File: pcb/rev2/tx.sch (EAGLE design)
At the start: 54 parts, among them U3 MCP73831T-2ACI/OT, Y1 CRYSTAL-26MHZSMD-3.2X2.5

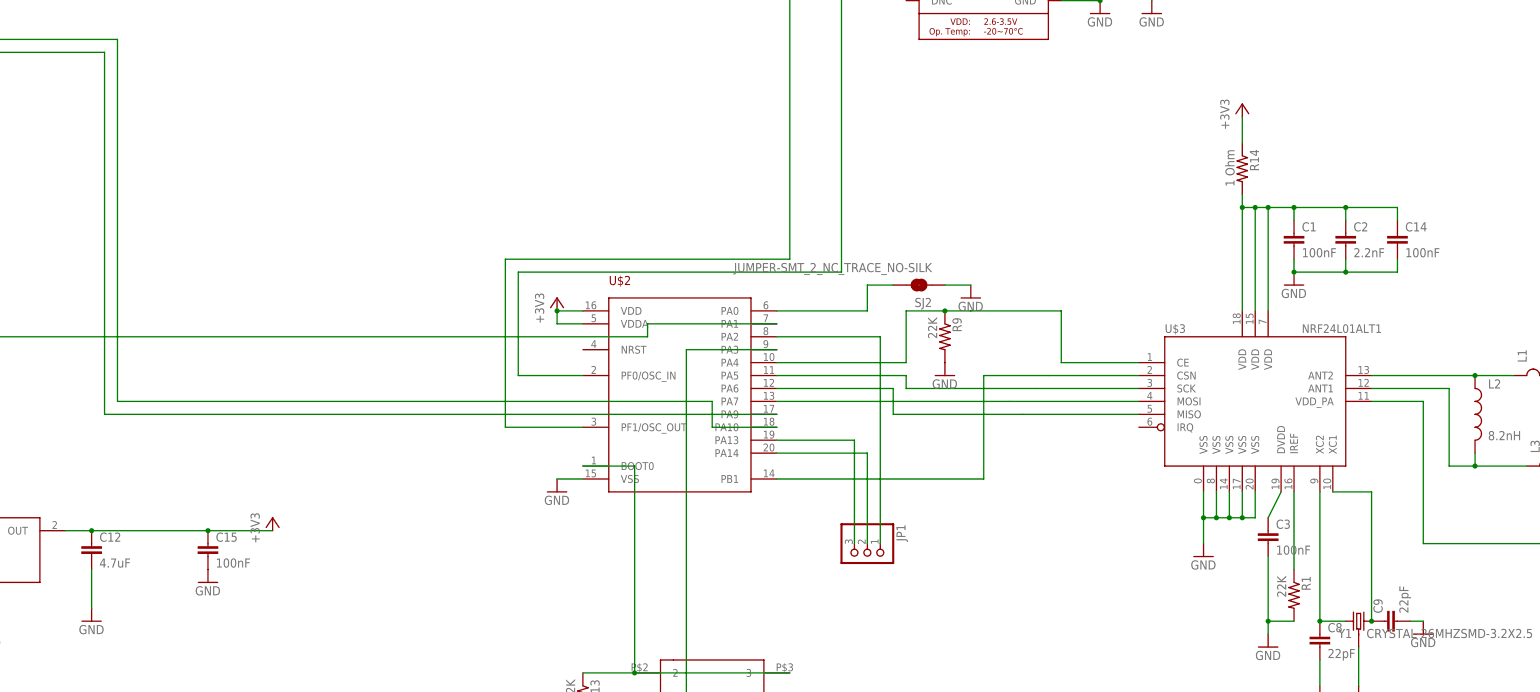
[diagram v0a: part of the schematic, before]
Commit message: added more power filtering, added RX interrupt
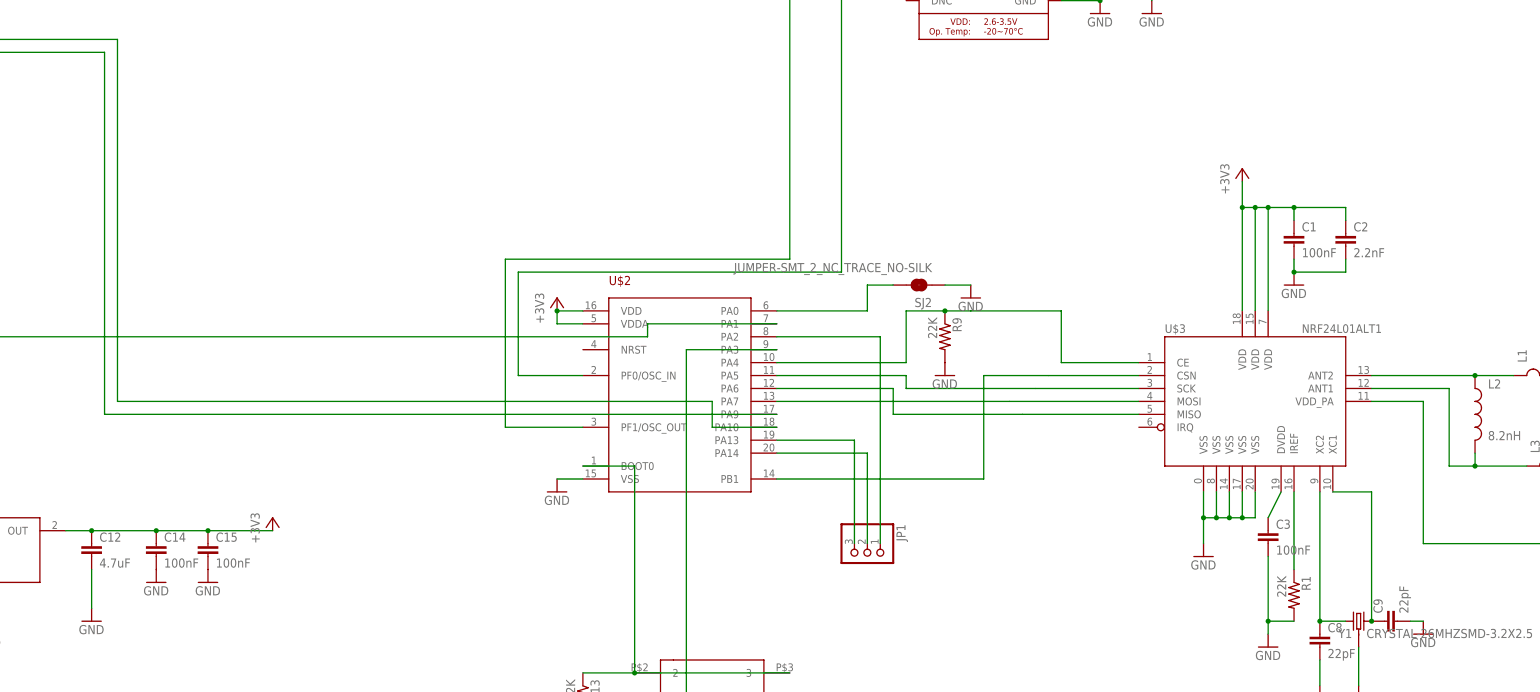
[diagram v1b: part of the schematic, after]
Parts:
- removed R14: 1 Ohm, joyAnalog:RESISTOR0805-RES
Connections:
- removed net N$37: C1.1, C14.1, C2.1, R14.2, U$3.VDD@15, U$3.VDD@18, U$3.VDD@7
- net +3V3: now also C1.1, C14.1, C2.1, U$3.VDD@15, U$3.VDD@18, U$3.VDD@7; no longer R14.1
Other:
- moved on the sheet: C14
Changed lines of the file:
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@@
 <part name="C14" library="clock" deviceset="CAP" device="0805" value="100nF"/>
 <part name="C15" library="clock" deviceset="CAP" device="0805" value="100nF"/>
+<part name="GND23" library="supply1" library_urn="urn:adsk.eagle:library:371" deviceset="GND" device=""/>
 <part name="GND24" library="supply1" library_urn="urn:adsk.eagle:library:371" deviceset="GND" device=""/>
 <part name="U$10" library="3pos_slide_switch" deviceset="324_SW" device="324_SWITCH_FOOT_HOLE" value="324_SW324_SWITCH_FOOT_HOLE"/>
@@
 <part name="U$13" library="3pos_slide_switch" deviceset="M2_SCREW_DEV" device=""/>
 <part name="U$14" library="3pos_slide_switch" deviceset="M2_SCREW_DEV" device=""/>
-<part name="R14" library="joyAnalog" deviceset="RESISTOR" device="0805-RES" value="1 Ohm"/>
 </parts>
 <sheets>
@@
 </instance>
 <instance part="U$3" gate="G$1" x="99.06" y="-60.96"/>
-<instance part="+3V1" gate="G$1" x="96.52" y="-2.54"/>
+<instance part="+3V1" gate="G$1" x="96.52" y="-15.24"/>
 <instance part="GND1" gate="1" x="88.9" y="-91.44"/>
 <instance part="C1" gate="G$1" x="106.68" y="-30.48"/>
@@
 <instance part="GND21" gate="1" x="-38.1" y="-78.74"/>
 <instance part="GND22" gate="1" x="-203.2" y="-76.2" rot="R180"/>
-<instance part="C14" gate="G$1" x="127" y="-30.48"/>
+<instance part="C14" gate="G$1" x="-116.84" y="-91.44"/>
 <instance part="C15" gate="G$1" x="-106.68" y="-91.44"/>
+<instance part="GND23" gate="1" x="-116.84" y="-96.52"/>
 <instance part="GND24" gate="1" x="-106.68" y="-96.52"/>
 <instance part="U$10" gate="G$1" x="-7.62" y="-119.38"/>
@@
 <instance part="U$13" gate="G$1" x="-116.84" y="-182.88"/>
 <instance part="U$14" gate="G$1" x="-157.48" y="-170.18"/>
-<instance part="R14" gate="G$1" x="96.52" y="-15.24" rot="R270"/>
 </instances>
 <busses>
@@
 <wire x1="116.84" y1="-35.56" x2="106.68" y2="-35.56" width="0.1524" layer="91"/>
 <junction x="106.68" y="-35.56"/>
-<pinref part="C14" gate="G$1" pin="2"/>
-<wire x1="127" y1="-33.02" x2="127" y2="-35.56" width="0.1524" layer="91"/>
-<wire x1="127" y1="-35.56" x2="116.84" y2="-35.56" width="0.1524" layer="91"/>
-<junction x="116.84" y="-35.56"/>
 </segment>
 <segment>
@@
 </segment>
 <segment>
+<pinref part="C14" gate="G$1" pin="2"/>
+<pinref part="GND23" gate="1" pin="GND"/>
+</segment>
+<segment>
 <pinref part="C15" gate="G$1" pin="2"/>
 <pinref part="GND24" gate="1" pin="GND"/>
@@
 </net>
 <net name="+3V3" class="0">
+<segment>
+<pinref part="+3V1" gate="G$1" pin="+3V3"/>
+<pinref part="U$3" gate="G$1" pin="VDD@18"/>
+<wire x1="96.52" y1="-17.78" x2="96.52" y2="-22.86" width="0.1524" layer="91"/>
+<pinref part="U$3" gate="G$1" pin="VDD@15"/>
+<wire x1="96.52" y1="-22.86" x2="96.52" y2="-43.18" width="0.1524" layer="91"/>
+<wire x1="96.52" y1="-22.86" x2="99.06" y2="-22.86" width="0.1524" layer="91"/>
+<wire x1="99.06" y1="-22.86" x2="99.06" y2="-43.18" width="0.1524" layer="91"/>
+<junction x="96.52" y="-22.86"/>
+<pinref part="U$3" gate="G$1" pin="VDD@7"/>
+<wire x1="99.06" y1="-22.86" x2="101.6" y2="-22.86" width="0.1524" layer="91"/>
+<wire x1="101.6" y1="-22.86" x2="101.6" y2="-43.18" width="0.1524" layer="91"/>
+<junction x="99.06" y="-22.86"/>
+<pinref part="C1" gate="G$1" pin="1"/>
+<wire x1="101.6" y1="-22.86" x2="106.68" y2="-22.86" width="0.1524" layer="91"/>
+<wire x1="106.68" y1="-22.86" x2="106.68" y2="-25.4" width="0.1524" layer="91"/>
+<junction x="101.6" y="-22.86"/>
+<pinref part="C2" gate="G$1" pin="1"/>
+<wire x1="106.68" y1="-22.86" x2="116.84" y2="-22.86" width="0.1524" layer="91"/>
+<wire x1="116.84" y1="-22.86" x2="116.84" y2="-25.4" width="0.1524" layer="91"/>
+<junction x="106.68" y="-22.86"/>
+</segment>
 <segment>
 <pinref part="U$9" gate="G$1" pin="OUT"/>
@@
 <wire x1="-134.62" y1="-86.36" x2="-129.54" y2="-86.36" width="0.1524" layer="91"/>
 <pinref part="C12" gate="G$1" pin="1"/>
+<wire x1="-129.54" y1="-86.36" x2="-116.84" y2="-86.36" width="0.1524" layer="91"/>
 <junction x="-129.54" y="-86.36"/>
+<pinref part="C14" gate="G$1" pin="1"/>
+<wire x1="-116.84" y1="-86.36" x2="-106.68" y2="-86.36" width="0.1524" layer="91"/>
+<junction x="-116.84" y="-86.36"/>
 <pinref part="C15" gate="G$1" pin="1"/>
 <wire x1="-106.68" y1="-86.36" x2="-93.98" y2="-86.36" width="0.1524" layer="91"/>
 <junction x="-106.68" y="-86.36"/>
-<wire x1="-129.54" y1="-86.36" x2="-106.68" y2="-86.36" width="0.1524" layer="91"/>
 </segment>
 <segment>
@@
 <wire x1="7.62" y1="-121.92" x2="15.24" y2="-121.92" width="0.1524" layer="91"/>
 <junction x="7.62" y="-121.92"/>
-</segment>
-<segment>
-<pinref part="+3V1" gate="G$1" pin="+3V3"/>
-<pinref part="R14" gate="G$1" pin="1"/>
-<wire x1="96.52" y1="-5.08" x2="96.52" y2="-10.16" width="0.1524" layer="91"/>
 </segment>
 </net>
@@
 </segment>
 </net>
-<net name="N$37" class="0">
-<segment>
-<pinref part="U$3" gate="G$1" pin="VDD@18"/>
-<pinref part="U$3" gate="G$1" pin="VDD@15"/>
-<wire x1="96.52" y1="-22.86" x2="96.52" y2="-43.18" width="0.1524" layer="91"/>
-<wire x1="96.52" y1="-22.86" x2="99.06" y2="-22.86" width="0.1524" layer="91"/>
-<wire x1="99.06" y1="-22.86" x2="99.06" y2="-43.18" width="0.1524" layer="91"/>
-<pinref part="U$3" gate="G$1" pin="VDD@7"/>
-<wire x1="99.06" y1="-22.86" x2="101.6" y2="-22.86" width="0.1524" layer="91"/>
-<wire x1="101.6" y1="-22.86" x2="101.6" y2="-43.18" width="0.1524" layer="91"/>
-<junction x="99.06" y="-22.86"/>
-<pinref part="C1" gate="G$1" pin="1"/>
-<wire x1="101.6" y1="-22.86" x2="106.68" y2="-22.86" width="0.1524" layer="91"/>
-<wire x1="106.68" y1="-22.86" x2="106.68" y2="-25.4" width="0.1524" layer="91"/>
-<junction x="101.6" y="-22.86"/>
-<pinref part="C2" gate="G$1" pin="1"/>
-<wire x1="106.68" y1="-22.86" x2="116.84" y2="-22.86" width="0.1524" layer="91"/>
-<wire x1="116.84" y1="-22.86" x2="116.84" y2="-25.4" width="0.1524" layer="91"/>
-<junction x="106.68" y="-22.86"/>
-<pinref part="R14" gate="G$1" pin="2"/>
-<wire x1="96.52" y1="-20.32" x2="96.52" y2="-22.86" width="0.1524" layer="91"/>
-<junction x="96.52" y="-22.86"/>
-<wire x1="116.84" y1="-22.86" x2="127" y2="-22.86" width="0.1524" layer="91"/>
-<junction x="116.84" y="-22.86"/>
-<pinref part="C14" gate="G$1" pin="1"/>
-<wire x1="127" y1="-22.86" x2="127" y2="-25.4" width="0.1524" layer="91"/>
-</segment>
-</net>
